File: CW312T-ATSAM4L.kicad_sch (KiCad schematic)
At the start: 30 parts, among them J1 614105150721, P1 PCIEx4 EDGE CONNECTOR, U1 ATSAM4LC2AA-AU

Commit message: updated schematic, pcb, and production files - ready for review
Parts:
- C3, C4, J1: now not fitted
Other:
- note removed: "C3, C4, J1 not mounted on default build. For USB build mount C3/C4/J1."
- note removed: "JP1 to use internal LDO on SAM4L"
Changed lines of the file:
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@@
 	)
 	(junction
+		(at 218.44 85.09)
+		(diameter 0)
+		(color 0 0 0 0)
+	)
+	(junction
 		(at 107.95 41.91)
 		(diameter 0)
@@
 	)
 	(junction
-		(at 229.87 85.09)
-		(diameter 0)
-		(color 0 0 0 0)
-	)
-	(junction
 		(at 31.75 77.47)
 		(diameter 0)
@@
 	(wire
 		(pts
-			(xy 218.44 90.17) (xy 218.44 80.01)
+			(xy 218.44 90.17) (xy 218.44 85.09)
 		)
 		(stroke
@@
 	(wire
 		(pts
+			(xy 218.44 85.09) (xy 229.87 85.09)
+		)
+		(stroke
+			(width 0)
+			(type default)
+		)
+	)
+	(wire
+		(pts
 			(xy 231.14 55.88) (xy 231.14 58.42)
 		)
@@
 	(wire
 		(pts
+			(xy 218.44 85.09) (xy 218.44 80.01)
+		)
+		(stroke
+			(width 0)
+			(type default)
+		)
+	)
+	(wire
+		(pts
 			(xy 224.79 71.12) (xy 231.14 71.12)
 		)
@@
 	(wire
 		(pts
+			(xy 215.9 85.09) (xy 218.44 85.09)
+		)
+		(stroke
+			(width 0)
+			(type default)
+		)
+	)
+	(wire
+		(pts
 			(xy 215.9 72.39) (xy 218.44 72.39)
 		)
@@
 	(wire
 		(pts
-			(xy 215.9 85.09) (xy 229.87 85.09)
-		)
-		(stroke
-			(width 0)
-			(type default)
-		)
-	)
-	(wire
-		(pts
 			(xy 83.82 62.23) (xy 95.25 62.23)
 		)
@@
 	(wire
 		(pts
-			(xy 229.87 81.28) (xy 229.87 85.09)
-		)
-		(stroke
-			(width 0)
-			(type default)
-		)
-	)
-	(wire
-		(pts
 			(xy 128.27 38.1) (xy 128.27 41.91)
 		)
@@
 		)
 	)
-	(text "JP1 to use internal LDO on SAM4L\n"
+	(text_box "JP1 to use internal LDO om SAM4L"
 		(exclude_from_sim no)
-		(at 263.652 102.108 0)
+		(at 245.11 97.79 0)
+		(size 36.83 3.81)
+		(stroke
+			(width 0)
+			(type default)
+		)
+		(fill
+			(type none)
+		)
 		(effects
 			(font
 				(size 1.27 1.27)
 			)
+			(justify top)
 		)
 	)
-	(text "C3, C4, J1 not mounted on default build. \nFor USB build mount C3/C4/J1. "
+	(text_box "C3, C4, and J1 not mounted on default build. \nFor USB build mount C3, C4, and J1"
 		(exclude_from_sim no)
-		(at 87.884 191.008 0)
+		(at 59.69 185.42 0)
+		(size 46.99 5.08)
+		(stroke
+			(width 0)
+			(type default)
+		)
+		(fill
+			(type none)
+		)
 		(effects
 			(font
 				(size 1.27 1.27)
 			)
+			(justify top)
 		)
 	)
@@
 	)
 	(symbol
-		(lib_id "power:+3V3")
-		(at 229.87 81.28 0)
-		(unit 1)
-		(exclude_from_sim no)
-		(in_bom yes)
-		(on_board yes)
-		(dnp no)
-		(property "Reference" "#PWR09"
-			(at 229.87 85.09 0)
-			(effects
-				(font
-					(size 1.27 1.27)
-				)
-				(hide yes)
-			)
-		)
-		(property "Value" "+3V3"
-			(at 229.87 77.216 0)
-			(effects
-				(font
-					(size 1.27 1.27)
-				)
-			)
-		)
-		(property "Footprint" ""
-			(at 229.87 81.28 0)
-			(effects
-				(font
-					(size 1.27 1.27)
-				)
-				(hide yes)
-			)
-		)
-		(property "Datasheet" ""
-			(at 229.87 81.28 0)
-			(effects
-				(font
-					(size 1.27 1.27)
-				)
-				(hide yes)
-			)
-		)
-		(property "Description" "Power symbol creates a global label with name \"+3V3\""
-			(at 229.87 81.28 0)
-			(effects
-				(font
-					(size 1.27 1.27)
-				)
-				(hide yes)
-			)
-		)
-		(pin "1"
-		)
-		(instances
-			(project ""
-				(path "/75376c85-aeac-4546-a639-110a257841a4"
-					(reference "#PWR09")
-					(unit 1)
-				)
-			)
-		)
-	)
-	(symbol
 		(lib_id "Silkscreen_Symbols:Pb_Free")
 		(at -35.56 160.02 0)
@@
 		(in_bom yes)
 		(on_board yes)
-		(dnp no)
+		(dnp yes)
 		(property "Reference" "C3"
 			(at 131.826 179.832 90)
@@
 		(in_bom yes)
 		(on_board yes)
-		(dnp no)
+		(dnp yes)
 		(property "Reference" "C4"
 			(at 140.716 179.832 90)
@@
 		(in_bom yes)
 		(on_board yes)
-		(dnp no)
+		(dnp yes)
 		(property "Reference" "J1"
 			(at 99.822 147.574 0)

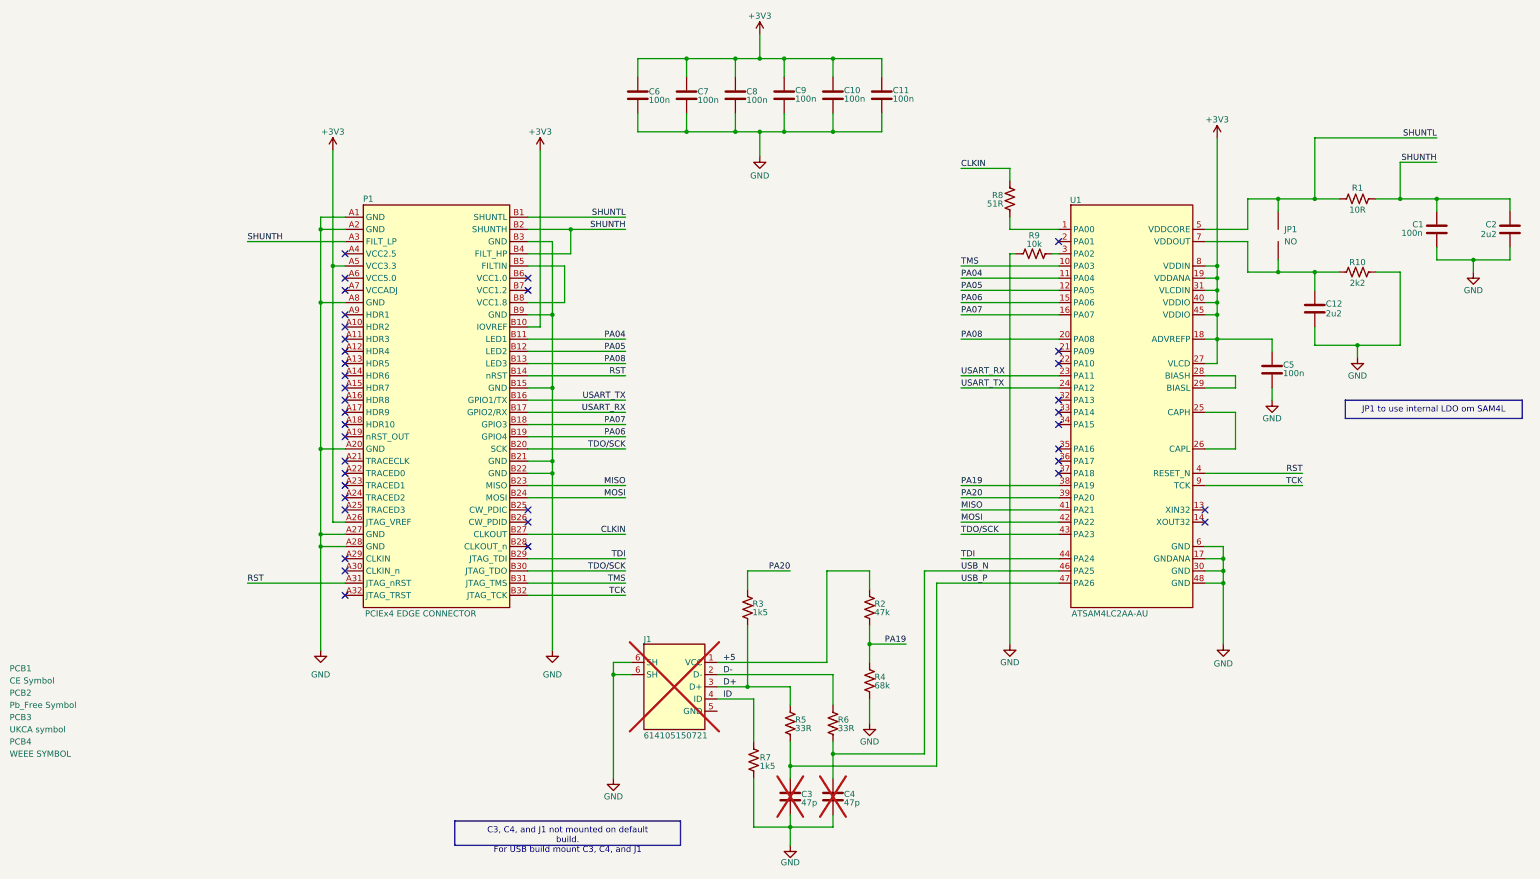
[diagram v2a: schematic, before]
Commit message: updated schematic and pcb after library re-organization
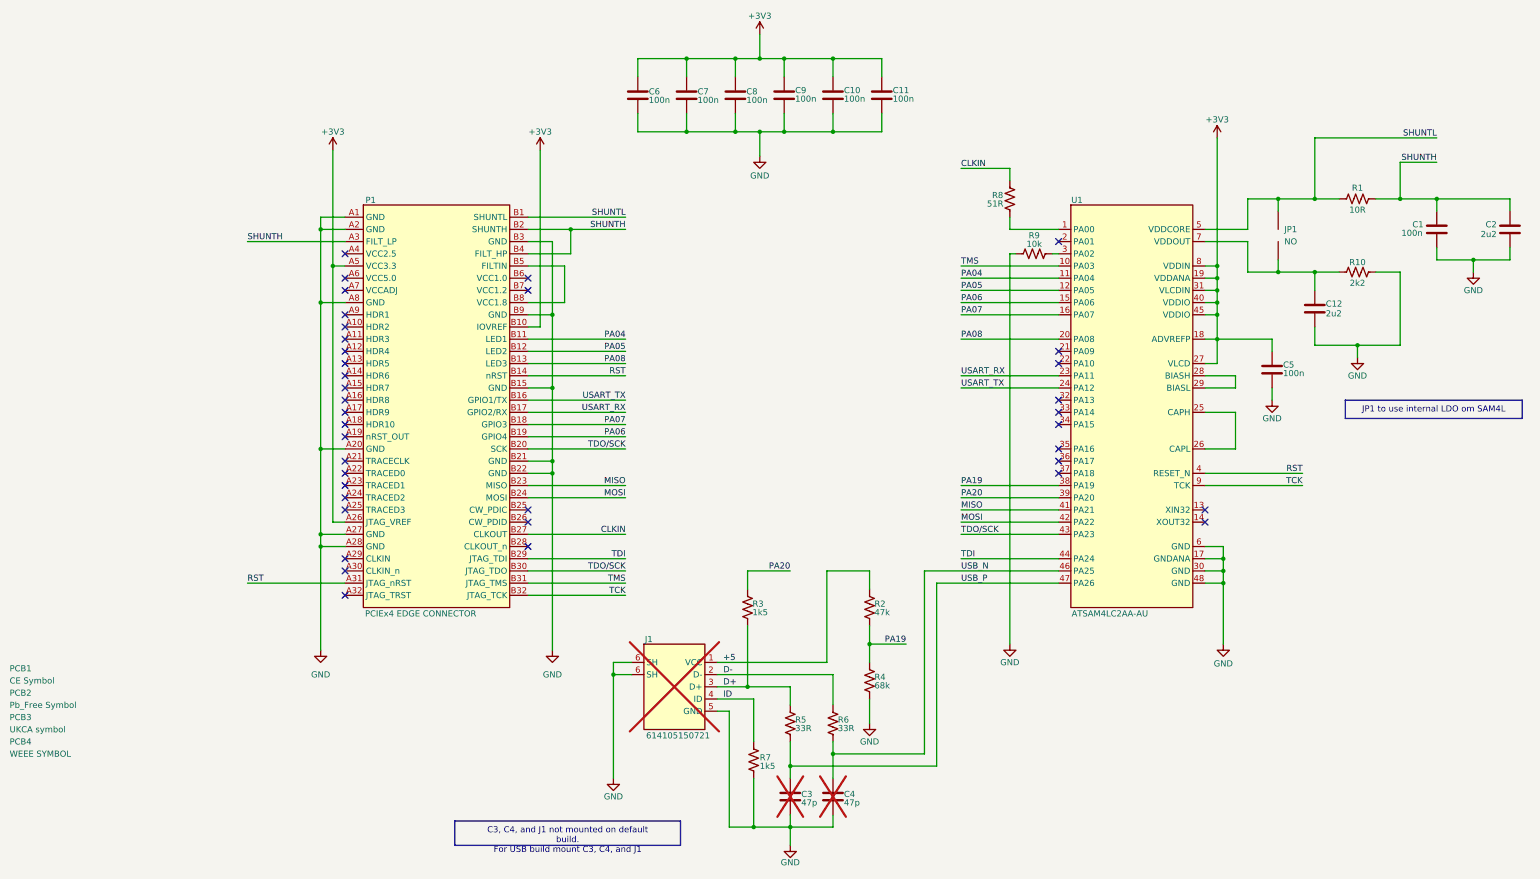
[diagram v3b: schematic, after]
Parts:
- removed J1: 614105150721, Connector_USB:USB_Micro-B_Wuerth_614105150721_Vertical, symbol tutorial_2_library:614105150721
- removed JP1: ~, Jumper:SolderJumper-2_P1.3mm_Open_Pad1.0x1.5mm, symbol tutorial_2_library:Solder_Jumper_2_NO
- removed P1: PCIEx4 EDGE CONNECTOR, tutorial_2_library:CW312_Template, symbol tutorial_2_library:CW312T-Template
- removed U1: ATSAM4LC2AA-AU, Package_QFP:LQFP-48_7x7mm_P0.5mm, symbol tutorial_2_library:ATSAM4LC2AA-AU
- added J1: 614105150721, Connector_USB:USB_Micro-B_Wuerth_614105150721_Vertical, symbol NAE_Connectors:614105150721
- added JP1: ~, Jumper:SolderJumper-2_P1.3mm_Open_Pad1.0x1.5mm, symbol NAE_Connectors:Solder_Jumper_2_NO
- added P1: PCIEx4 EDGE CONNECTOR, tutorial_2_library:CW312_Template, symbol NAE_Connectors:CW312T-Template
- added U1: ATSAM4LC2AA-AU, Package_QFP:LQFP-48_7x7mm_P0.5mm, symbol NAE_Integrated_Circuits:ATSAM4LC2AA-AU
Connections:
- net +3V3: now also P1.A26 (JTAG_VREF), P1.A5 (VCC3.3), P1.B10 (IOVREF), U1.18 (ADVREFP), U1.19 (VDDANA), U1.27 (VLCD), U1.31 (VLCDIN), U1.40 (VDDIO), U1.45 (VDDIO), U1.8 (VDDIN)
- net +5: now also J1.1 (VCC)
- net CLKIN: now also P1.B27 (CLKOUT)
- net D+: now also J1.3 (D+)
- net D-: now also J1.2 (D-)
- net GND: now also J1.5 (GND), J1.6 (SH), P1.A1 (GND), P1.A2 (GND), P1.A20 (GND), P1.A27 (GND), P1.A28 (GND), P1.A8 (GND), P1.B15 (GND), P1.B21 (GND), P1.B22 (GND), P1.B3 (GND), P1.B9 (GND), U1.17 (GNDANA), U1.30 (GND), U1.48 (GND), U1.6 (GND)
- net ID: now also J1.4 (ID)
- net MISO: now also P1.B23 (MISO), U1.41 (PA21)
- net MOSI: now also P1.B24 (MOSI), U1.42 (PA22)
- net PA04: now also P1.B11 (LED1), U1.11 (PA04)
- net PA05: now also P1.B12 (LED2), U1.12 (PA05)
- net PA06: now also P1.B19 (GPIO4), U1.15 (PA06)
- net PA07: now also P1.B18 (GPIO3), U1.16 (PA07)
- net PA08: now also P1.B13 (LED3), U1.20 (PA08)
- net PA19: now also U1.38 (PA19)
- net PA20: now also U1.39 (PA20)
- net RST: now also P1.A31 (JTAG_nRST), P1.B14 (nRST), U1.4 (RESET_N)
- net SHUNTH: now also P1.A3 (FILT_LP), P1.B2 (SHUNTH), P1.B4 (FILT_HP)
- net SHUNTL: now also JP1.2, P1.B1 (SHUNTL), U1.5 (VDDCORE)
- net TCK: now also P1.B32 (JTAG_TCK), U1.9 (TCK)
- net TDI: now also P1.B29 (JTAG_TDI), U1.44 (PA24)
- net TDO/SCK: now also P1.B20 (SCK), P1.B30 (JTAG_TDO), U1.43 (PA23)
- net TMS: now also P1.B31 (JTAG_TMS), U1.10 (PA03)
- net USART_RX: now also P1.B17 (GPIO2/RX), U1.23 (PA11)
- net USART_TX: now also P1.B16 (GPIO1/TX), U1.24 (PA12)
- net USB_N: now also U1.46 (PA25)
- net USB_P: now also U1.47 (PA26)
- net at C12.1, R10.1: now also JP1.1, U1.7 (VDDOUT)
- net at R9.2: now also U1.3 (PA02)
- net at R8.1: now also U1.1 (PA00)
- new net: P1.B5 (FILTIN), P1.B8 (VCC1.8)
- new net: U1.25 (CAPH), U1.26 (CAPL)
- new net: U1.28 (BIASH), U1.29 (BIASL)
